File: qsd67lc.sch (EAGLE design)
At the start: 54 parts, among them CON1 RIA-AKL-230-04, CON2 RIA-AKL-230-04, CON3 RIA-AKL-230-03, IC1 MEGA8-P, IC2 BTS555E3146, IC3 MAX3232CPE, IC4 LM2576S, IC5 FT232RL, T1 BCR141, U1 HC_05, X2 RS232

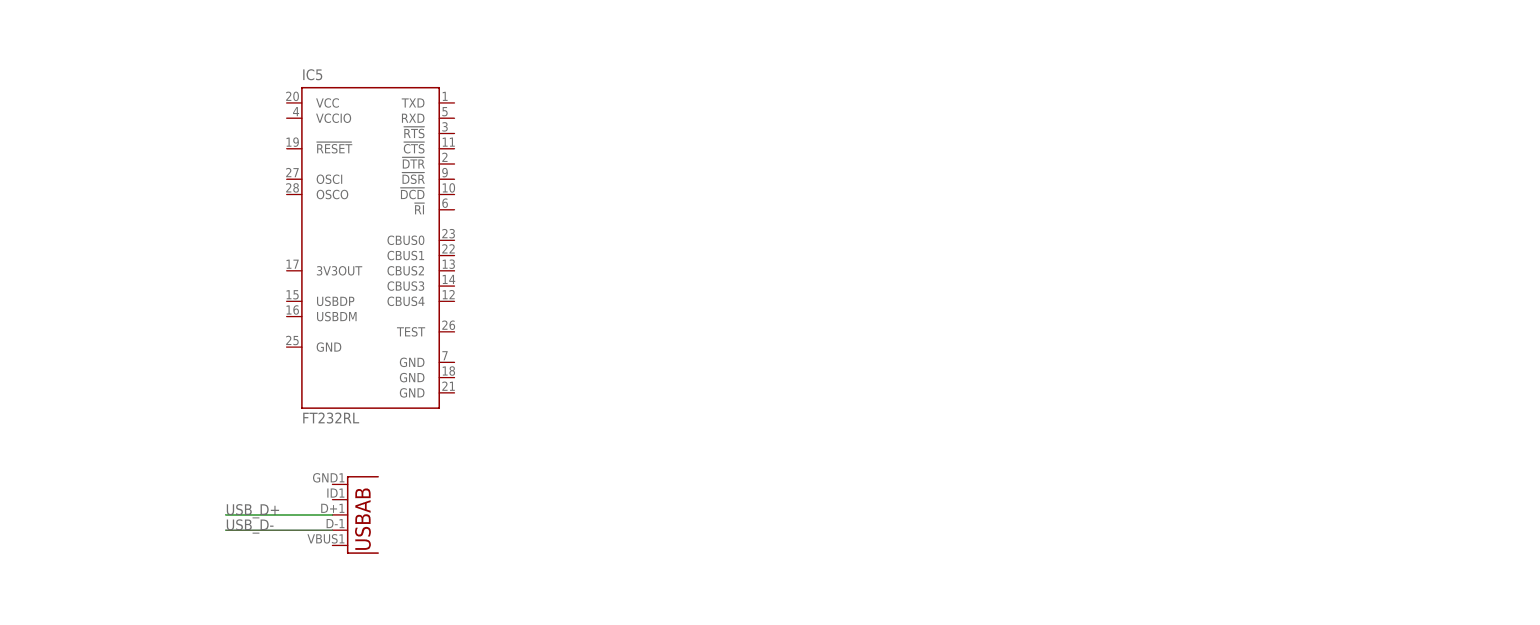
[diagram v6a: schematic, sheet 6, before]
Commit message: added galvanic decoupling for usb completed ftdi circuit
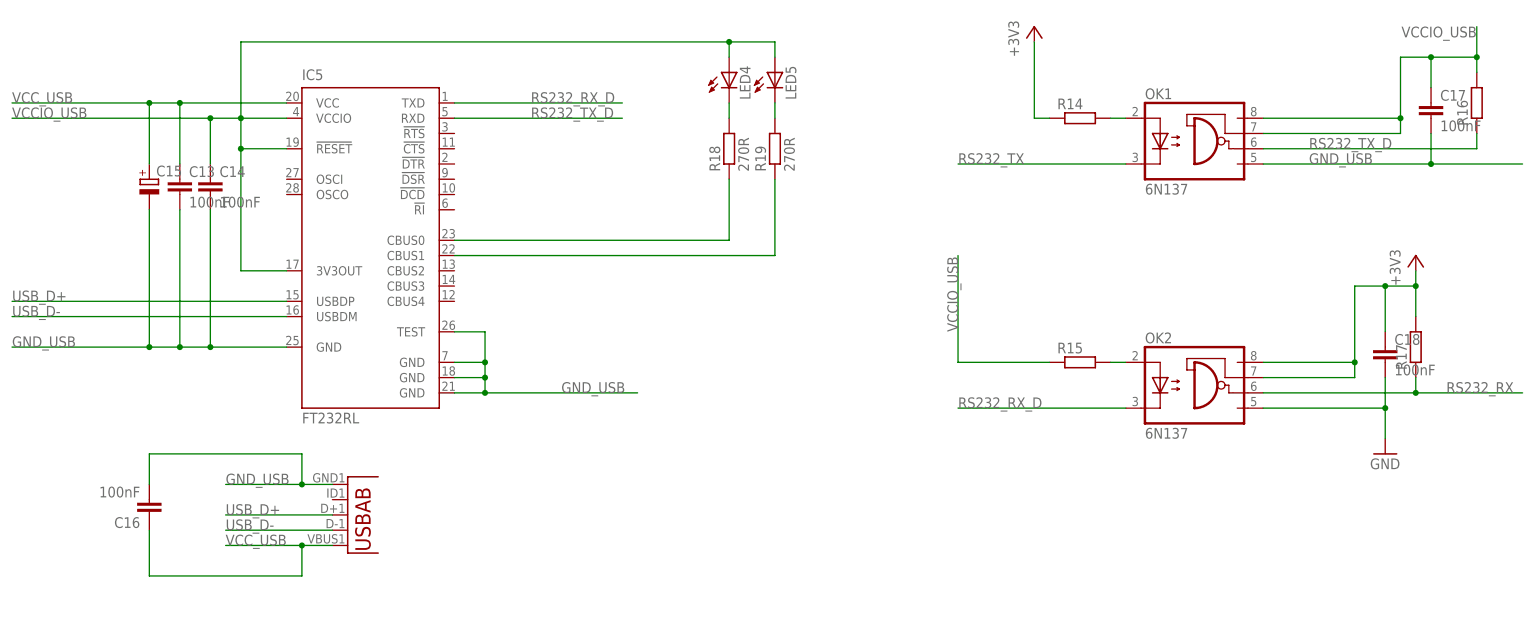
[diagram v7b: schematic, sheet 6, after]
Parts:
- added C13, C14, C16, C17, C18: 100nF, rcl:C-EUC0805
- added C15: (no value), rcl:CPOL-EUE2.5-5
- added LED4, LED5: (no value), led:LEDSML0805
- added OK1, OK2: 6N137, optocoupler:6N137
- added R14, R15, R16, R17: (no value), rcl:R-EU_R0805
- added R18, R19: 270R, rcl:R-EU_R0805
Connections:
- new net GND_USB: C13.2, C14.2, C15.-, C16.2, C17.2, IC5.GND, IC5.GND@1, IC5.GND@2, IC5.GND@A, IC5.TEST, OK1.GND, U2.GND
- new net N$10: OK2.A, R15.2
- new net N$21: OK1.A, R14.2
- new net N$23: LED4.C, R18.2
- new net N$25: IC5.CBUS1, R19.1
- new net N$26: LED5.C, R19.2
- new net RS232_RX_D: IC5.TXD, OK2.C
- new net RS232_TX_D: IC5.RXD, OK1.VO, R16.1
- new net USB_RX_LED: IC5.CBUS0, R18.1
- new net VCCIO_USB: C14.1, C17.1, IC5.!RESET, IC5.3V3OUT, IC5.VCCIO, LED4.A, LED5.A, OK1.VCC, OK1.VE, R15.1, R16.2
- new net VCC_USB: C13.1, C15.+, C16.1, IC5.VCC, U2.VBUS
- net +3V3: now also C18.1, OK2.VCC, OK2.VE, R14.1, R17.2
- net GND: now also C18.2, OK2.GND
- net RS232_RX: now also OK2.VO, R17.1
- net RS232_TX: now also OK1.C
- net USB_D+: now also IC5.USBDP
- net USB_D-: now also IC5.USBDM

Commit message: replaced the 6n137 by an iso7221 because of 3V3 compatibility
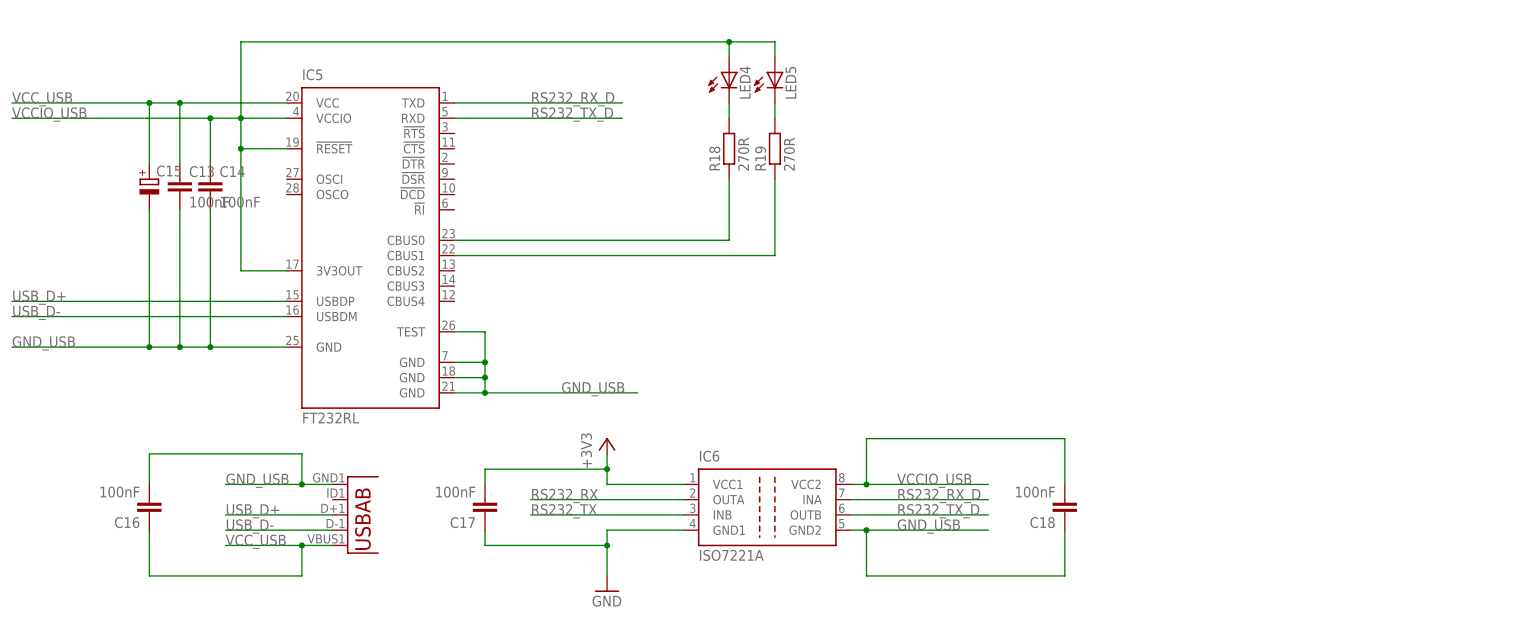
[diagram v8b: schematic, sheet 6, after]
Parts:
- removed OK1, OK2: 6N137, optocoupler:6N137
- removed R14, R15, R16, R17: (no value), rcl:R-EU_R0805
- added IC6: ISO7221A, texas:ISO7221A
- C12: value (none) -> 100nF
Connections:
- removed net N$10: OK2.A, R15.2
- removed net N$21: OK1.A, R14.2
- net +3V3: now also C17.2, IC6.VCC1; no longer C18.1, OK2.VCC, OK2.VE, R14.1, R17.2
- net GND: now also C17.1, IC6.GND1; no longer C18.2, OK2.GND
- net GND_USB: now also C18.1, IC6.GND2; no longer C17.2, OK1.GND
- net RS232_RX: now also IC6.OUTA; no longer OK2.VO, R17.1
- net RS232_RX_D: now also IC6.INA; no longer OK2.C
- net RS232_TX: now also IC6.INB; no longer OK1.C
- net RS232_TX_D: now also IC6.OUTB; no longer OK1.VO, R16.1
- net VCCIO_USB: now also C18.2, IC6.VCC2; no longer C17.1, OK1.VCC, OK1.VE, R15.1, R16.2
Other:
- moved on the sheet: C17, C18
